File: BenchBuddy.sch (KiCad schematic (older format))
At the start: 0 parts

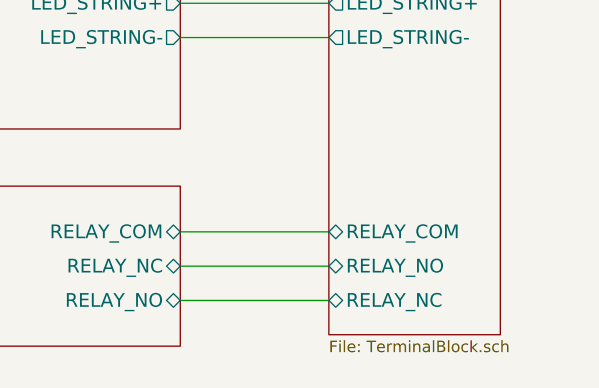
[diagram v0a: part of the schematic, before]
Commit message: Cleanup to schematic after doing a scale printout
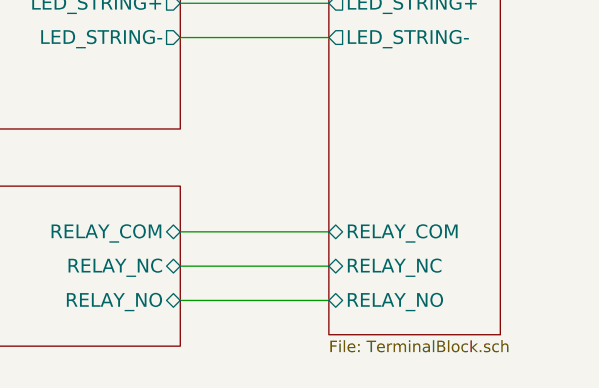
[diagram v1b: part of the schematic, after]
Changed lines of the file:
@@
-EESchema Schematic File Version 2  date 10/31/2013 9:00:44 PM
+EESchema Schematic File Version 2  date 11/2/2013 7:04:39 PM
 LIBS:power
 LIBS:device
@@
 Sheet 1 9
 Title "noname.sch"
-Date "1 nov 2013"
+Date "2 nov 2013"
 Rev ""
 Comp ""
@@
 F10 "TC_IN-" I L 10150 4050 60
 F11 "RELAY_COM" B L 10150 6100 60
-F12 "RELAY_NO" B L 10150 6250 60
-F13 "RELAY_NC" B L 10150 6400 60
+F12 "RELAY_NO" B L 10150 6400 60
+F13 "RELAY_NC" B L 10150 6250 60
 $EndSheet
 Wire Wire Line
@@
 	10150 6100 9500 6100
 Wire Wire Line
+	10150 6400 9500 6400
+Wire Wire Line
 	9500 6250 10150 6250
-Wire Wire Line
-	10150 6400 9500 6400
 $EndSCHEMATC
